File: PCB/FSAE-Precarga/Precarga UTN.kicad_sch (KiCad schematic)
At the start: 24 parts, among them J1 39310040, J4 39310040, J5 39310040, J7 39310040, K1 RER02, K2 RER02, Q1 IRF640S, Q3 IRF640S, U13 PC817, U9 PC817

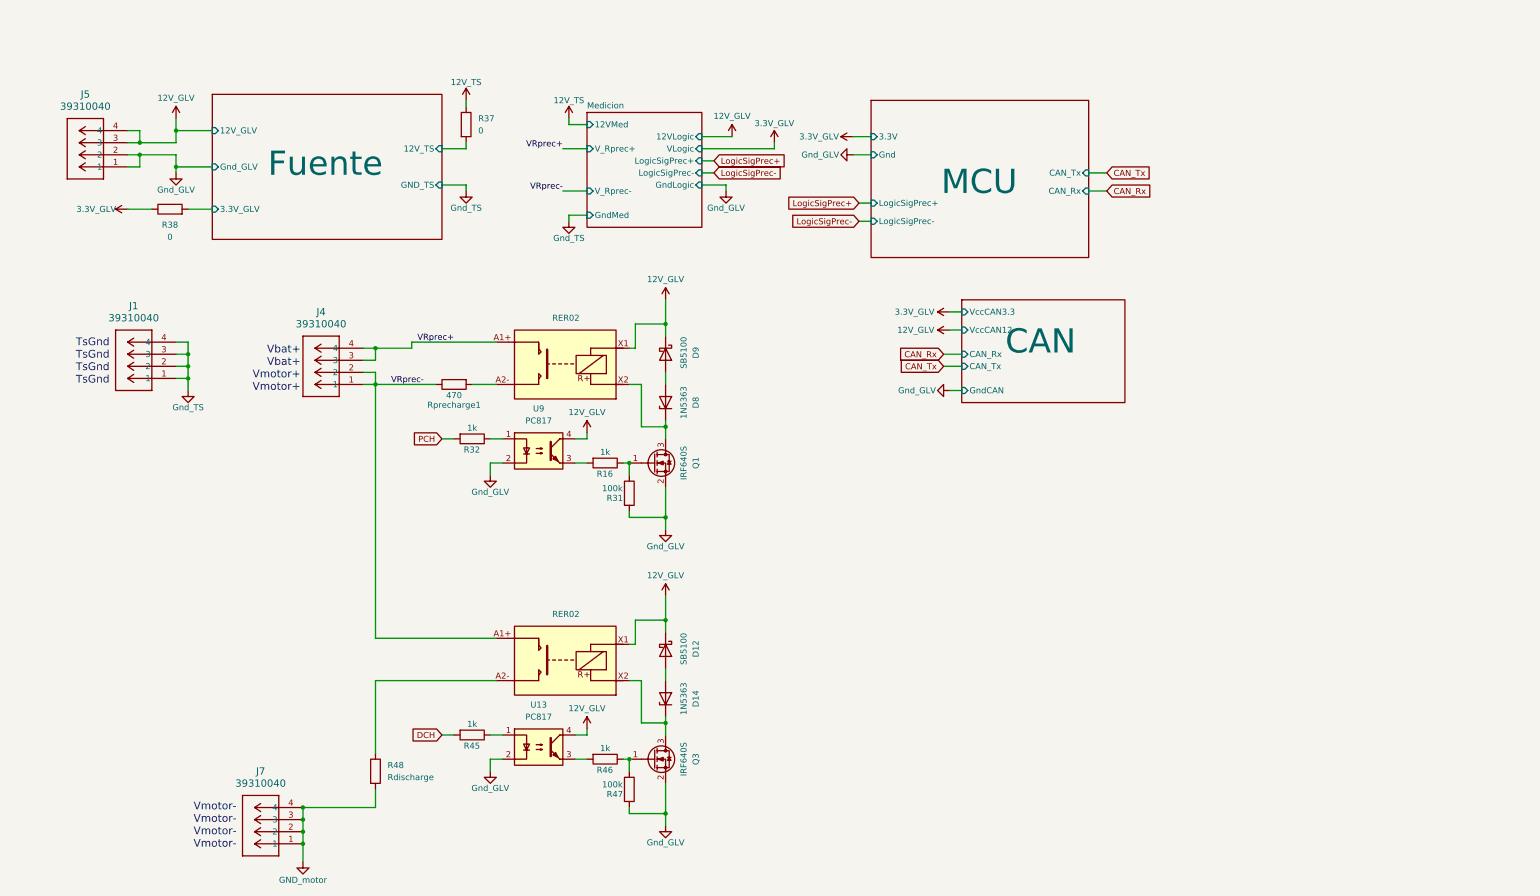
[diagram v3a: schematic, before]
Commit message: Agrego circuito de control/verificacion de los AIR en placa de precarga
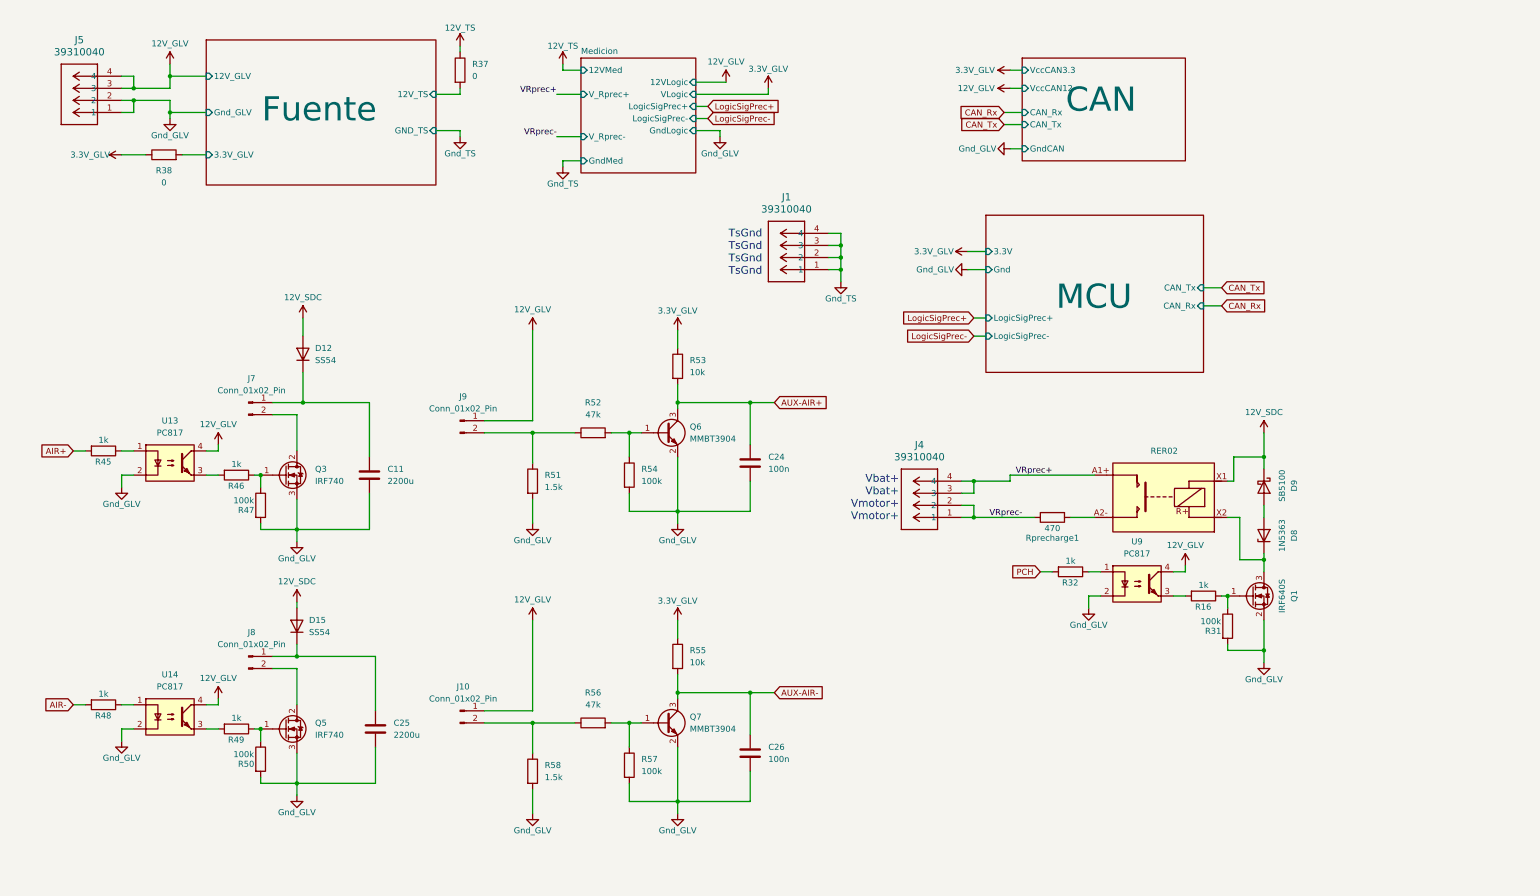
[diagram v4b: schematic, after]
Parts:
- removed D12: SB5100, Diode_THT:D_DO-41_SOD81_P10.16mm_Horizontal, symbol Diode:SB5H100
- removed D14: 1N5363, Diode_THT:D_DO-41_SOD81_P10.16mm_Horizontal, symbol Diode:1N53xxB
- removed J7: 39310040, CONN_SD-5566-002_04_MOL, symbol 2026-08-15_23-43-52:39310040
- removed K2: RER02, Mis_Huellas:RER02PAX, symbol MisSimbolos:RER02-Series
- removed Q3: IRF640S, Package_TO_SOT_SMD:TO-263-2, symbol Transistor_FET:AO3400A
- added C11, C25: 2200u, Capacitor_THT:CP_Radial_D13.0mm_P5.00mm, symbol Device:C
- added C24, C26: 100n, symbol Device:C
- added D12, D15: SS54, Diode_SMD:D_SMA, symbol Device:D
- added J10, J7, J8, J9: Conn_01x02_Pin, symbol Connector:Conn_01x02_Pin
- added Q3, Q5: IRF740, Package_TO_SOT_THT:TO-220-3_Vertical, symbol Transistor_FET:IRF740
- added Q6, Q7: MMBT3904, Package_TO_SOT_SMD:SOT-23, symbol Transistor_BJT:MMBT3904
- added R49: 1k, Resistor_SMD:R_0603_1608Metric, symbol Device:R
- added R50: 100k, Resistor_SMD:R_0603_1608Metric, symbol Device:R
- added R51, R58: 1.5k, symbol Device:R
- added R52, R56: 47k, symbol Device:R
- added R53, R55: 10k, symbol Device:R
- added R54, R57: 100k, symbol Device:R
- added U14: PC817, Package_DIP:DIP-4_W7.62mm_SMDSocket_SmallPads, symbol Isolator:PC817
- R48: value Rdischarge -> 1k; footprint (none) -> Resistor_SMD:R_0603_1608Metric
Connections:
- net 12V_GLV: now also J10.1 (Pin_1), J9.1 (Pin_1), U14.4; no longer D9.1 (K), K1.X1
- net 3.3V_GLV: now also R53.1, R55.1
- net Gnd_GLV: now also C11.2, C24.2, C25.2, C26.2, Q3.3 (S), Q5.3 (S), Q6.2 (E), Q7.2 (E), R50.2, R51.2, R54.2, R57.2, R58.2, U14.2
- net at R46.1, R47.1: now also Q3.1 (G)
- net at R48.1: now also U14.1
- net DCH renamed AIR+
- net GND_motor renamed AIR-
- new net: C25.1, D15.1 (K), J8.1 (Pin_1)
- new net: J9.2 (Pin_2), R51.1, R52.1
- new net: Q6.1 (B), R52.2, R54.1
- new net: J10.2 (Pin_2), R56.1, R58.1
- new net: Q7.1 (B), R56.2, R57.1
- new net: J8.2 (Pin_2), Q5.2 (D)
- new net: C11.1, D12.1 (K), J7.1 (Pin_1)
- new net: J7.2 (Pin_2), Q3.2 (D)
- new net: Q5.1 (G), R49.1, R50.1
- new net: R49.2, U14.3
- new net 12V_SDC: D12.2 (A), D15.2 (A), D9.1 (K), K1.X1
- new net AUX-AIR+: C24.1, Q6.3 (C), R53.2
- new net AUX-AIR-: C26.1, Q7.3 (C), R55.2
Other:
- note removed: "Vmotor- Vmotor- Vmotor- Vmotor-"
- moved on the sheet: D8, D9, J1, J4, J5, Q1, R16, R31, R32, R37, R38, Rprecharge1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
